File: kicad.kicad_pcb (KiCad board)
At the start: 2 copper layers, 39 parts, among them J1 Screw_Terminal_01x02, J2 Screw_Terminal_01x03, J4 Screw_Terminal_01x03, K1 SANYOU_SRD_Form_C, K2 SANYOU_SRD_Form_C, Q1 BC817, Q2 BC817, Q3 BC817, Q4 BC817, Q5 IRF540N, U1 4N25, U2 4N25, U3 4N25, U4 4N25, U5 LM2575-5.0BT, U6 ACS759xCB-050B-PFF

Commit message: various updates
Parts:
- added C1: 100nF, Capacitor_SMD:C_1206_3216Metric_Pad1.33x1.80mm_HandSolder, F.Cu at (134.6, 96.5)
- added C10: 470uF, Capacitor_SMD:CP_Elec_10x10, F.Cu at (75.9, 70.6)
- added C10A1: ALT, Capacitor_THT:CP_Radial_D10.0mm_P3.80mm, F.Cu at (138.0, 74.8)
- added C11: 470uF, Capacitor_SMD:CP_Elec_10x10, F.Cu at (75.9, 82.5)
- added C11A1: ALT, Capacitor_THT:CP_Radial_D10.0mm_P3.80mm, F.Cu at (141.3, 62.9)
- added C12: 470uF, Capacitor_SMD:CP_Elec_10x10, F.Cu at (92.7, 65.8)
- added C12A1: ALT, Capacitor_THT:CP_Radial_D10.0mm_P3.80mm, F.Cu at (126.2, 74.8)
- added C13: 100uF, Capacitor_THT:CP_Radial_D6.3mm_P2.50mm, F.Cu at (171.9, 105.4)
- added C14: 100nF, Capacitor_SMD:C_1206_3216Metric_Pad1.33x1.80mm_HandSolder, F.Cu at (185.9, 47.3)
- added C15: 100nF, Capacitor_SMD:C_1206_3216Metric_Pad1.33x1.80mm_HandSolder, F.Cu at (177.5, 53.7)
- added C16: 100nF, Capacitor_SMD:C_1206_3216Metric_Pad1.33x1.80mm_HandSolder, F.Cu at (177.5, 57.1)
- added C17: 1nF, Capacitor_SMD:C_1206_3216Metric_Pad1.33x1.80mm_HandSolder, F.Cu at (183.5, 53.7)
- added C18: 100nF, Capacitor_SMD:C_1206_3216Metric_Pad1.33x1.80mm_HandSolder, F.Cu at (217.1, 114.8)
- added C19: 100nF, Capacitor_SMD:C_1206_3216Metric_Pad1.33x1.80mm_HandSolder, F.Cu at (217.1, 118.2)
- added C2: 22pF, Capacitor_SMD:C_1206_3216Metric_Pad1.33x1.80mm_HandSolder, F.Cu at (147.1, 111.6)
- added C20: 100nF, Capacitor_SMD:C_1206_3216Metric_Pad1.33x1.80mm_HandSolder, F.Cu at (195.3, 137.2)
- added C21: 100nF, Capacitor_SMD:C_1206_3216Metric_Pad1.33x1.80mm_HandSolder, F.Cu at (195.3, 133.9)
- added C5A1: ALT, Capacitor_THT:CP_Radial_D10.0mm_P3.80mm, F.Cu at (129.5, 63.2)
- added C6A1: ALT, Capacitor_THT:CP_Radial_D10.0mm_P3.80mm, F.Cu at (114.4, 77.5)
- added C7: 100nF, Capacitor_SMD:C_1206_3216Metric_Pad1.33x1.80mm_HandSolder, F.Cu at (71.6, 90.1)
- added C8: 470uF, Capacitor_SMD:CP_Elec_10x10, F.Cu at (90.0, 77.6)
- added C8A1: ALT, Capacitor_THT:CP_Radial_D10.0mm_P3.80mm, F.Cu at (102.9, 77.5)
- added C9: 470uF, Capacitor_SMD:CP_Elec_10x10, F.Cu at (108.3, 51.5)
- added C9A1: ALT, Capacitor_THT:CP_Radial_D10.0mm_P3.80mm, F.Cu at (133.3, 51.4)
- added D10: LED, LED_SMD:LED_1206_3216Metric, F.Cu at (168.1, 124.6)
- added D11: 1N4007, Diode_THT:D_DO-41_SOD81_P7.62mm_Horizontal, F.Cu at (167.2, 120.7)
- added D12: LED, LED_SMD:LED_1206_3216Metric, F.Cu at (208.1, 81.8)
- added D13: 1N4007, Diode_THT:D_DO-41_SOD81_P7.62mm_Horizontal, F.Cu at (207.1, 77.9)
- added D14: BAT54S, Package_TO_SOT_SMD:SOT-23, F.Cu at (106.8, 140.9)
- added D15: BAT54S, Package_TO_SOT_SMD:SOT-23, F.Cu at (91.6, 140.9)
- added D16: BAT54S, Package_TO_SOT_SMD:SOT-23, F.Cu at (76.4, 140.9)
- added D5: LED, LED_SMD:LED_1206_3216Metric, F.Cu at (229.2, 51.5)
- added D6: LED, LED_SMD:LED_1206_3216Metric, F.Cu at (143.8, 47.3)
- added D7: SS14, Diode_SMD:D_SMA_Handsoldering, F.Cu at (115.3, 85.5)
- added D7A1: ALT, Diode_THT:D_DO-201_P12.70mm_Horizontal, F.Cu at (70.6, 61.3)
- added D8: 1N4007, Diode_THT:D_DO-41_SOD81_P7.62mm_Horizontal, F.Cu at (228.2, 47.7)
- added D9: BAT54S, Package_TO_SOT_SMD:SOT-23, F.Cu at (122.0, 140.9)
- added H1: MountingHole_Pad, MountingHole:MountingHole_4mm_Pad_Via, F.Cu at (161.3, -31.8)
- added H2: MountingHole_Pad, MountingHole:MountingHole_4mm_Pad_Via, F.Cu at (146.1, -31.8)
- added J10: Conn_01x06, Connector_Molex:Molex_KK-254_AE-6410-06A_1x06_P2.54mm_Vertical, F.Cu at (184.9, 122.6)
- added J3: Screw_Terminal_01x03, TerminalBlock:TerminalBlock_bornier-3_P5.08mm, F.Cu at (101.4, 115.2)
- added J5: Screw_Terminal_01x03, TerminalBlock:TerminalBlock_bornier-3_P5.08mm, F.Cu at (101.4, 106.1)
- added J6: USB_B, Connector_USB:USB_B_TE_5787834_Vertical, F.Cu at (153.7, 99.9)
- added J7: Conn_01x03, Connector_Molex:Molex_KK-254_AE-6410-03A_1x03_P2.54mm_Vertical, F.Cu at (206.7, 117.1)
- added J8: Conn_01x03, Connector_Molex:Molex_KK-254_AE-6410-03A_1x03_P2.54mm_Vertical, F.Cu at (184.9, 136.1)
- added J9: Conn_01x03, Connector_Molex:Molex_KK-254_AE-6410-03A_1x03_P2.54mm_Vertical, F.Cu at (167.7, 79.8)
- added JP1: SolderJumper_2_Open, Jumper:SolderJumper-2_P1.3mm_Open_RoundedPad1.0x1.5mm, F.Cu at (107.9, 87.0)
- added JP2: SolderJumper_3_Bridged12, Jumper:SolderJumper-3_P1.3mm_Open_RoundedPad1.0x1.5mm_NumberLabels, F.Cu at (191.8, 47.4)
- added JP3: SolderJumper_2_Bridged, Jumper:SolderJumper-2_P1.3mm_Open_RoundedPad1.0x1.5mm, F.Cu at (235.6, 90.1)
- added JP4: SolderJumper_2_Bridged, Jumper:SolderJumper-2_P1.3mm_Open_RoundedPad1.0x1.5mm, F.Cu at (220.3, 107.1)
- added JP5: SolderJumper_2_Bridged, Jumper:SolderJumper-2_P1.3mm_Open_RoundedPad1.0x1.5mm, F.Cu at (235.6, 76.9)
- added K3: RELAY, Relay_THT:Relay_SPDT_SANYOU_SRD_Series_Form_C, F.Cu at (186.1, 84.3)
- added L1: 68uH, Inductor_SMD:L_12x12mm_H8mm, F.Cu at (57.1, 38.1)
- added L1A1: ALT, Inductor_THT:L_Radial_D12.0mm_P5.00mm_Fastron_11P, F.Cu at (54.6, 38.1)
- added Q6: BC817, Package_TO_SOT_SMD:SOT-23, F.Cu at (167.3, 85.9)
- added Q7: IRF540N, Package_TO_SOT_THT:TO-220-3_Vertical, F.Cu at (157.1, 79.7)
- added Q8: BC817, Package_TO_SOT_SMD:SOT-23, F.Cu at (197.1, 107.6)
- added R15: 1k, Resistor_SMD:R_1206_3216Metric, F.Cu at (183.3, 57.0)
- added R16: 1k, Resistor_SMD:R_1206_3216Metric, F.Cu at (143.8, 50.6)
- added R17: 330, Resistor_SMD:R_1206_3216Metric, F.Cu at (143.8, 53.9)
- added R18: 1k, Resistor_SMD:R_1206_3216Metric, F.Cu at (117.0, 143.6)
- added R19: 1k, Resistor_SMD:R_1206_3216Metric, F.Cu at (117.0, 140.3)
- added R20: 2k, Resistor_SMD:R_1206_3216Metric, F.Cu at (177.3, 60.4)
- added R21: 1k, Resistor_SMD:R_1206_3216Metric, F.Cu at (101.8, 140.3)
- added R22: 1k, Resistor_SMD:R_1206_3216Metric, F.Cu at (101.8, 143.6)
- added R23: 1k, Resistor_SMD:R_1206_3216Metric, F.Cu at (86.6, 140.3)
- added R24: 1k, Resistor_SMD:R_1206_3216Metric, F.Cu at (86.6, 143.6)
- added R25: 1k, Resistor_SMD:R_1206_3216Metric, F.Cu at (71.4, 143.6)
- added R26: 1k, Resistor_SMD:R_1206_3216Metric, F.Cu at (71.4, 140.3)
- added R27: 1k, Resistor_SMD:R_1206_3216Metric, F.Cu at (156.6, 83.4)
- added R28: 10k, Resistor_SMD:R_1206_3216Metric, F.Cu at (162.2, 85.3)
- added R29: 1k, Resistor_SMD:R_1206_3216Metric, F.Cu at (197.7, 103.7)
- added R30: 10k, Resistor_SMD:R_1206_3216Metric, F.Cu at (197.7, 100.4)
- added R31: 1k, Resistor_SMD:R_1206_3216Metric, F.Cu at (236.2, 86.7)
- added R32: 10k, Resistor_SMD:R_1206_3216Metric, F.Cu at (236.2, 83.4)
- added R33: 1k, Resistor_SMD:R_1206_3216Metric, F.Cu at (220.9, 103.7)
- added R34: 10k, Resistor_SMD:R_1206_3216Metric, F.Cu at (220.9, 100.4)
- added R35: 1k, Resistor_SMD:R_1206_3216Metric, F.Cu at (236.2, 73.5)
- added R36: 10k, Resistor_SMD:R_1206_3216Metric, F.Cu at (236.2, 70.2)
- added SW1: SW_Push, Button_Switch_THT:SW_PUSH_6mm, F.Cu at (116.8, 115.0)
- added SW2: SW_Push, Button_Switch_THT:SW_PUSH_6mm, F.Cu at (128.3, 105.9)
- added U10: 4N25, Package_DIP:DIP-6_W7.62mm, F.Cu at (224.2, 70.6)
- added U7: LM2596S-3.3, Package_TO_SOT_SMD:TO-263-5_TabPin3, F.Cu at (77.5, 22.9)
- added U7A1: ALT, Package_TO_SOT_THT:TO-220-5_Vertical, F.Cu at (85.0, 87.5)
- added U8: 4N25, Package_DIP:DIP-6_W7.62mm, F.Cu at (208.9, 100.8)
- added U9: LM7805, Package_TO_SOT_THT:TO-220-3_Vertical, F.Cu at (97.4, 89.2)
- added Y1: 12MHz, Crystal:Crystal_HC49-4H_Vertical, F.Cu at (164.8, 98.2)
- C3: value 100nF -> 22pF
- C5, C6: value 100nF -> 470uF; footprint Capacitor_SMD:C_1206_3216Metric_Pad1.33x1.80mm_HandSolder -> Capacitor_SMD:CP_Elec_10x10
- D1, D2: value 1N4007 -> SS14; footprint Diode_THT:D_DO-41_SOD81_P7.62mm_Horizontal -> Diode_SMD:D_SMA_Handsoldering
- D3: value 1N5822 -> ALT
- D4: value 1N4007 -> ALT; footprint Diode_THT:D_DO-41_SOD81_P7.62mm_Horizontal -> Diode_THT:D_DO-201_P12.70mm_Horizontal
- J4: value Screw_Terminal_01x03 -> Conn_01x05; footprint TerminalBlock:TerminalBlock_bornier-3_P5.08mm -> Connector_Molex:Molex_KK-254_AE-6410-05A_1x05_P2.54mm_Vertical
- K1, K2: value SANYOU_SRD_Form_C -> RELAY
- Q5: value IRF540N -> BC817; footprint Package_TO_SOT_THT:TO-220-3_Vertical -> Package_TO_SOT_SMD:SOT-23
- R1, R13, R2: value 1k -> 10k; footprint Resistor_SMD:R_1206_3216Metric_Pad1.30x1.75mm_HandSolder -> Resistor_SMD:R_1206_3216Metric
- R10, R11, R9: footprint Resistor_SMD:R_1206_3216Metric_Pad1.30x1.75mm_HandSolder -> Resistor_SMD:R_1206_3216Metric
- R12, R14: value 10K -> 10k; footprint Resistor_SMD:R_1206_3216Metric_Pad1.30x1.75mm_HandSolder -> Resistor_SMD:R_1206_3216Metric
- R3: value 22k -> 1k; footprint Resistor_SMD:R_0805_2012Metric_Pad1.20x1.40mm_HandSolder -> Resistor_SMD:R_1206_3216Metric
- R4: value 5k6 -> 1k; footprint Resistor_SMD:R_0805_2012Metric_Pad1.20x1.40mm_HandSolder -> Resistor_SMD:R_1206_3216Metric
- R5: value 10k -> 22k; footprint Resistor_SMD:R_1206_3216Metric_Pad1.30x1.75mm_HandSolder -> Resistor_SMD:R_1206_3216Metric
- R6: value 10k -> 5k6; footprint Resistor_SMD:R_1206_3216Metric_Pad1.30x1.75mm_HandSolder -> Resistor_SMD:R_1206_3216Metric
- R7, R8: value 10k -> 1k; footprint Resistor_SMD:R_1206_3216Metric_Pad1.30x1.75mm_HandSolder -> Resistor_SMD:R_1206_3216Metric
- U1: value 4N25 -> CH340G; footprint Package_DIP:DIP-6_W7.62mm -> Package_SO:SOIC-16_3.9x9.9mm_P1.27mm
- U2: value 4N25 -> ACS759; footprint Package_DIP:DIP-6_W7.62mm -> Sensor_Current:Allegro_CB_PFF
- U3: value 4N25 -> ACS712; footprint Package_DIP:DIP-6_W7.62mm -> Package_SO:SOIC-8_3.9x4.9mm_P1.27mm
- U5: value LM2575-5.0BT -> 4N25; footprint Package_TO_SOT_THT:TO-220-5_Vertical -> Package_DIP:DIP-6_W7.62mm
- U6: value ACS759xCB-050B-PFF -> ESP32; footprint Sensor_Current:Allegro_CB_PFF -> RF_Module:ESP32-WROOM-32
- moved RV1 155.5 mm to (77.5, 90.0)
- moved U3 149.2 mm to (153.7, -14.0), turned to 270 degrees
- moved U2 146.5 mm to (151.7, 0.00)
- moved D3 135.9 mm to (70.6, 130.8)
- moved R5 132.1 mm to (103.0, 130.5)
- moved C6 131.3 mm to (106.8, 65.8)
- moved C5 122.2 mm to (122.4, 51.5)
- moved R2 115.9 mm to (114.2, 132.7)
- moved J1 104.4 mm to (118.0, 108.4)
- moved R11 104.2 mm to (108.6, 132.7)
- moved R6 104.0 mm to (103.0, 133.8)
- moved D1 97.0 mm to (103.1, 122.0)
- moved J4 96.9 mm to (87.7, 131.3)
- moved R3 93.5 mm to (234.8, 51.5)
- moved D4 93.2 mm to (100.2, 98.2)
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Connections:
- net Net-(J2-Pad1) renamed /Relay 1/NO
- net Net-(J2-Pad2) renamed /Relay 1/COM
- net Net-(J2-Pad3) renamed /Relay 1/NC
- C3 pad 1: +3V3 -> Net-(C3-Pad1)
- C4 pad 1: /TBAT -> +3V3
- C5 pad 1: Net-(C5-Pad1) -> +12V
- C6 pad 1: /TEMP2 -> +12V
- D1 pad 2: Net-(D1-Pad2) -> VUSB
- D3 pad 1: Net-(D3-Pad1) -> +12V
- D3 pad 2: GND -> Net-(D2-Pad2)
- D4 pad 2: Net-(D4-Pad2) -> VUSB
- J1 pad 1: Net-(D1-Pad2) -> Net-(D2-Pad2)
- J4 pad 1: Net-(J4-Pad1) -> SCL
- J4 pad 2: Net-(J4-Pad2) -> SDA
- J4 pad 3: Net-(J4-Pad3) -> +3V3
- K1 pad 2: Net-(D2-Pad2) -> Net-(D8-Pad2)
- K2 pad 1: Net-(J4-Pad2) -> /Relay 2/COM
- K2 pad 2: Net-(D4-Pad2) -> Net-(D11-Pad2)
- K2 pad 3: Net-(J4-Pad1) -> /Relay 2/NO
- K2 pad 4: Net-(J4-Pad3) -> /Relay 2/NC
- Q1 pad 3: Net-(Q1-Pad3) -> Net-(D8-Pad2)
- Q2 pad 3: Net-(D2-Pad2) -> Net-(D11-Pad2)
- Q3 pad 3: Net-(D4-Pad2) -> Net-(D13-Pad2)
- Q4 pad 2: GND -> Net-(Q4-Pad2)
- Q4 pad 3: Net-(Q4-Pad3) -> GPIO0
- Q5 pad 1: Net-(Q4-Pad3) -> Net-(Q5-Pad1)
- Q5 pad 2: Net-(J5-Pad3) -> Net-(Q5-Pad2)
- Q5 pad 3: GND -> RESET
- R1 pad 1: Net-(Q1-Pad1) -> +3V3
- R1 pad 2: /UPS_ON -> RESET
- R10 pad 1: Net-(Q4-Pad1) -> Net-(Q3-Pad1)
- R10 pad 2: /FAN_1 -> RELAY_3
- R11 pad 1: +12V -> +3V3
- R11 pad 2: Net-(Q4-Pad3) -> SDA
- R12 pad 2: /SDA -> SCL
- R13 pad 1: /IBAT -> Net-(Q4-Pad1)
- R13 pad 2: Net-(C5-Pad1) -> Net-(Q5-Pad2)
- R14 pad 1: +3V3 -> Net-(Q5-Pad1)
- R14 pad 2: /SCL -> Net-(Q4-Pad2)
- R2 pad 1: Net-(Q2-Pad1) -> +3V3
- R2 pad 2: /RELAY_1 -> GPIO0
- R3 pad 1: +12V -> Net-(D5-Pad1)
- R3 pad 2: /VBAT -> Net-(D8-Pad2)
- R4 pad 1: /VBAT -> Net-(Q1-Pad1)
- R4 pad 2: GND -> RELAY_1
- R5 pad 1: +3V3 -> +12V
- R5 pad 2: Net-(Q1-Pad3) -> /Input Protection/IN
- R6 pad 1: /UPS_NORMAL -> /Input Protection/IN
- R6 pad 2: +3V3 -> GND
- R7 pad 1: /UPS_CARGA -> Net-(D10-Pad1)
- R7 pad 2: +3V3 -> Net-(D11-Pad2)
- R8 pad 1: /UPS_INVERTER -> Net-(Q2-Pad1)
- R8 pad 2: +3V3 -> RELAY_2
- R9 pad 1: Net-(Q3-Pad1) -> Net-(D12-Pad1)
- R9 pad 2: /RELAY_2 -> Net-(D13-Pad2)
- U1 pad 1: Net-(Q1-Pad3) -> GND
- U1 pad 2: GND -> RXD0
- U1 pad 3: Net-(U1-Pad3) -> TXD0
- U1 pad 4: Net-(J3-Pad2) -> +3V3
- U2 pad 1: Net-(J3-Pad4) -> +3V3
- U2 pad 2: Net-(J3-Pad3) -> GND
- U2 pad 4: GND -> /Current Sensor/IP+
- U2 pad 5: /UPS_NORMAL -> /Current Sensor/IP-
- U3 pad 1: Net-(J3-Pad4) -> /Current Sensor/IP+
- U3 pad 2: Net-(J3-Pad5) -> /Current Sensor/IP+
- U3 pad 3: Net-(U3-Pad3) -> /Current Sensor/IP-
- U3 pad 4: GND -> /Current Sensor/IP-
- U3 pad 5: /UPS_CARGA -> GND
- U4 pad 1: Net-(J3-Pad4) -> Net-(Q8-Pad3)
- U4 pad 2: Net-(J3-Pad6) -> GND
- U4 pad 4: GND -> /Interfaz UPS/Salida UPS_ON/E
- U4 pad 5: /UPS_INVERTER -> /Interfaz UPS/Salida UPS_ON/C
- U5 pad 1: +12V -> Net-(JP3-Pad2)
- U5 pad 2: Net-(D3-Pad1) -> /Interfaz UPS/Entrada UPS_NORMAL/K
- U5 pad 3: GND -> Net-(U5-Pad3)
- U5 pad 4: Net-(JP1-Pad2) -> GND
- U5 pad 5: GND -> UPS_NORMAL
- U6 pad 1: +3V3 -> GND
- U6 pad 2: GND -> +3V3
- U6 pad 3: Net-(C5-Pad1) -> RESET
- U6 pad 4: Net-(H1-Pad1) -> VBAT
- U6 pad 5: Net-(H2-Pad1) -> TBAT

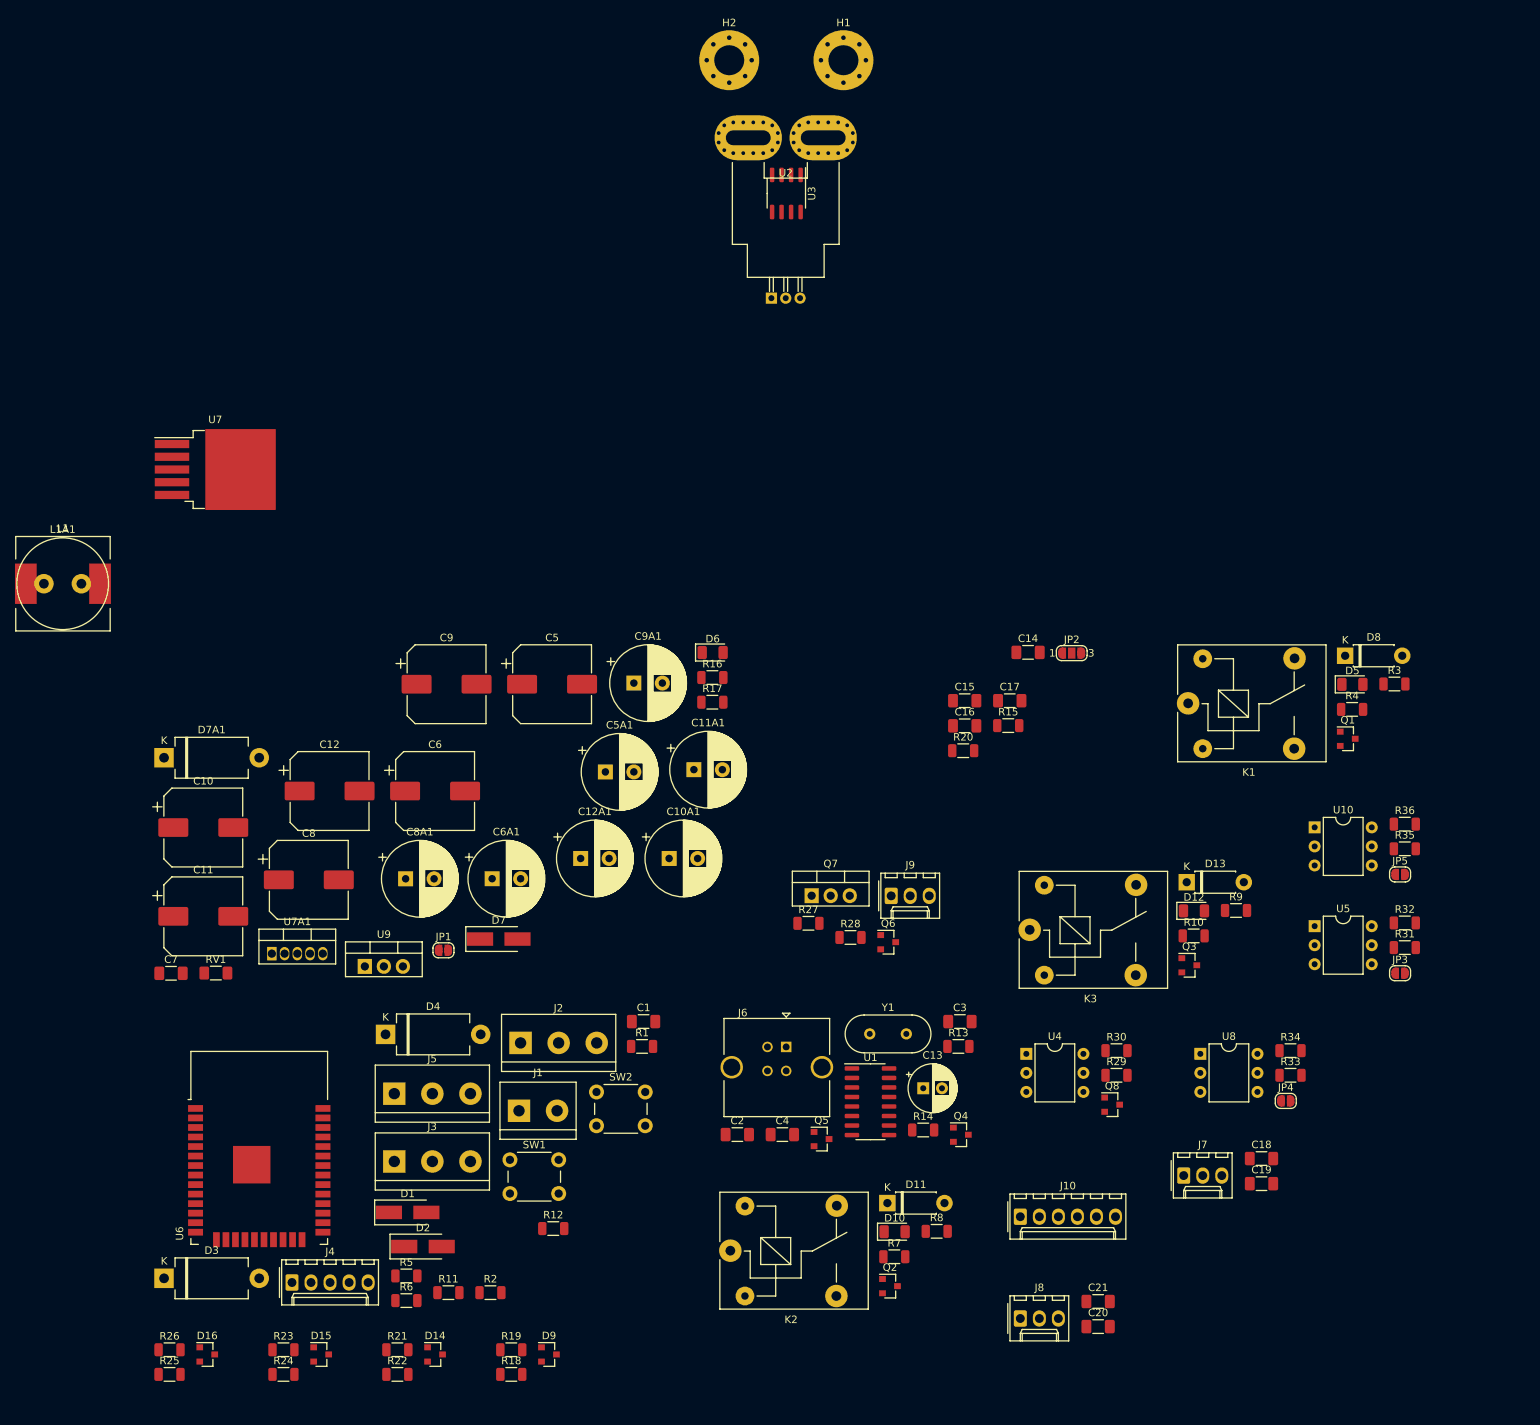
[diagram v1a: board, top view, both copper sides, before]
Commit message: more footprints & 3d models
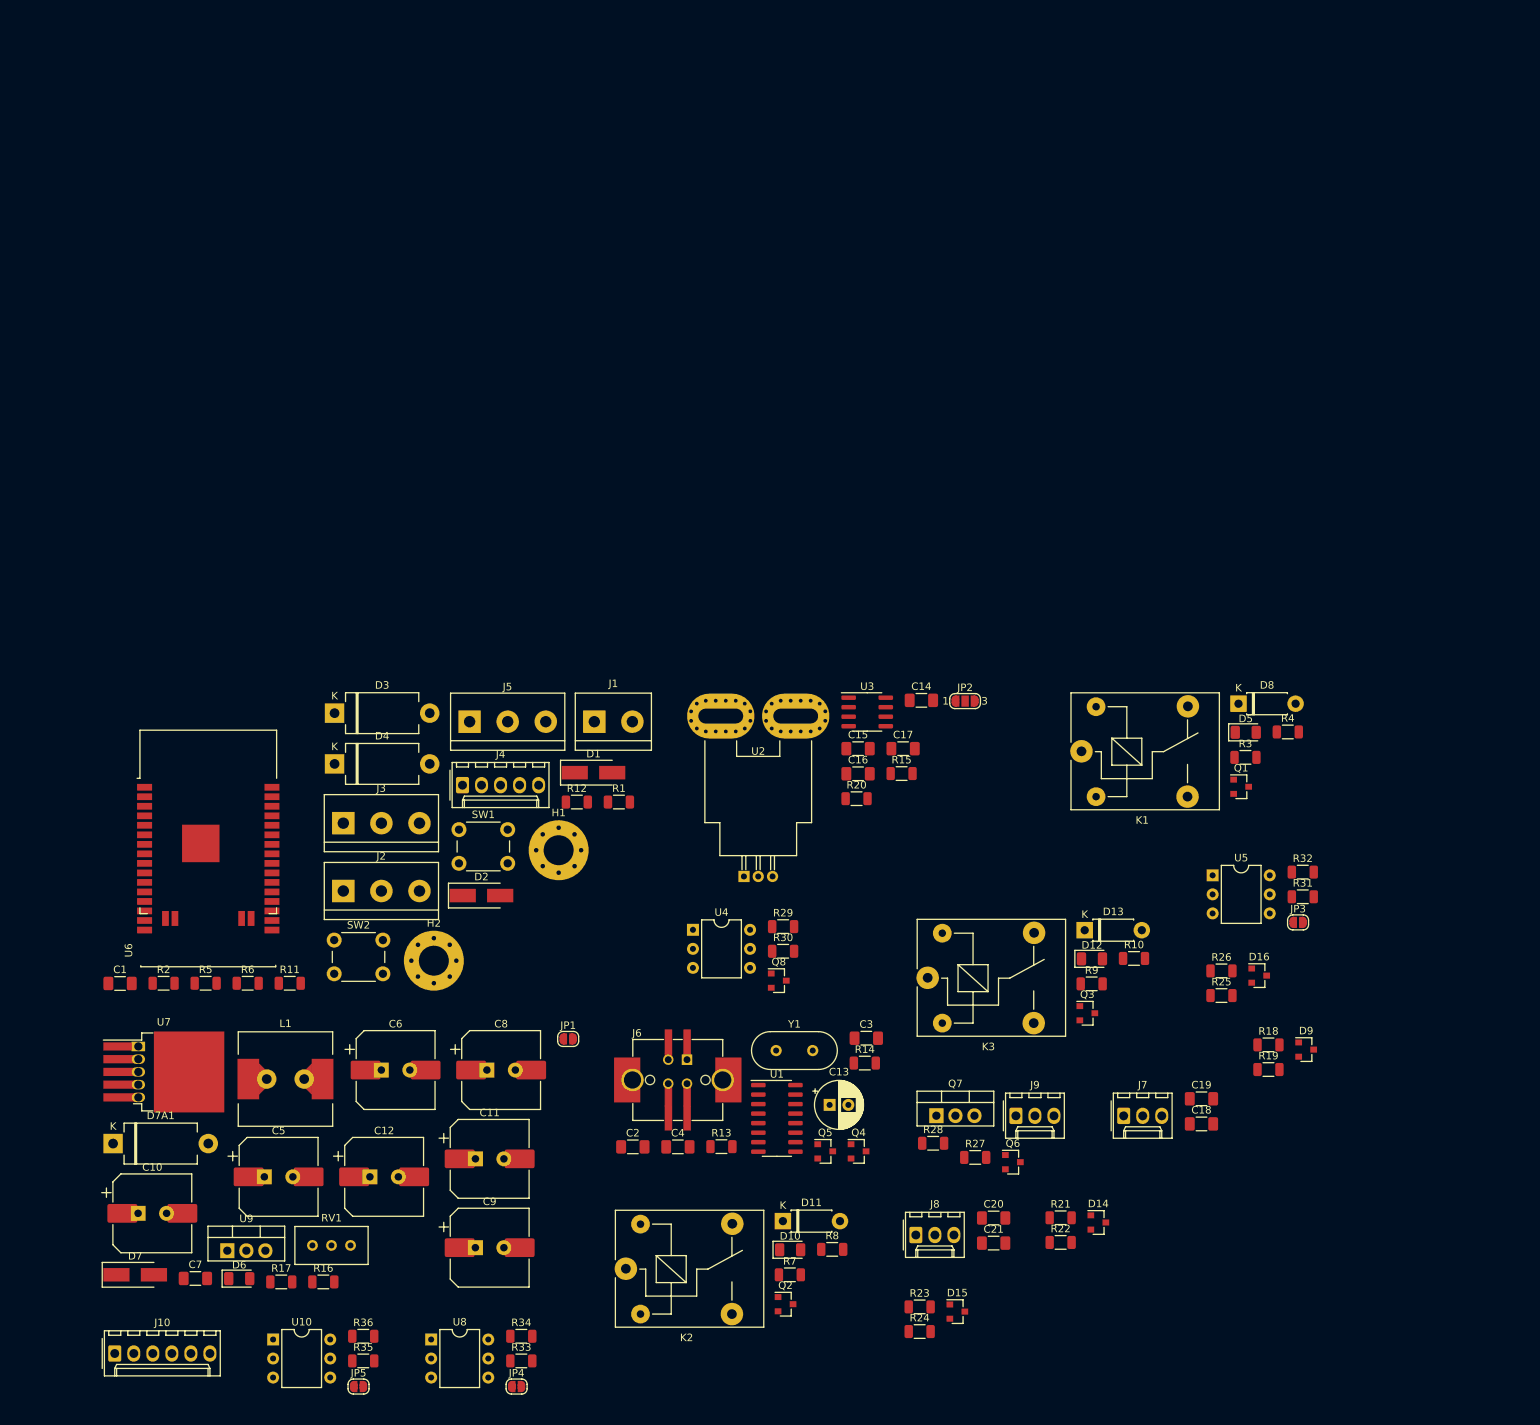
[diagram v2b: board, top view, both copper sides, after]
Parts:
- removed C10A1, C11A1, C12A1, C5A1, C6A1, C8A1, C9A1: ALT, Capacitor_THT:CP_Radial_D10.0mm_P3.80mm
- removed L1A1: ALT, Inductor_THT:L_Radial_D12.0mm_P5.00mm_Fastron_11P
- removed U7A1: ALT, Package_TO_SOT_THT:TO-220-5_Vertical
- C10, C11, C12, C5, C6, C8, C9: footprint Capacitor_SMD:CP_Elec_10x10 -> libs:CAP_10x10_SMD_THT
- J1: footprint TerminalBlock:TerminalBlock_bornier-2_P5.08mm -> libs:TerminalBlock_bornier-2_P5.08mm
- J2, J3, J5: footprint TerminalBlock:TerminalBlock_bornier-3_P5.08mm -> libs:TerminalBlock_bornier-3_P5.08mm
- J6: footprint Connector_USB:USB_B_TE_5787834_Vertical -> libs:USB-B-VERTICAL-SMD&THT
- L1: footprint Inductor_SMD:L_12x12mm_H8mm -> libs:L_12x12mm_H8mm
- RV1: footprint Resistor_SMD:R_1206_3216Metric_Pad1.30x1.75mm_HandSolder -> Potentiometer_THT:Potentiometer_Bourns_3296W_Vertical
- U2: footprint Sensor_Current:Allegro_CB_PFF -> libs:Allegro_CB_PFF
- U6: footprint RF_Module:ESP32-WROOM-32 -> esp32-wroom-roover:ESP32-WROOM-WROVER-NC
- U7: footprint Package_TO_SOT_SMD:TO-263-5_TabPin3 -> libs:TO-263-5_TabPin3
- moved R35 154.9 mm to (97.2, 141.8)
- moved JP5 154.9 mm to (96.6, 145.2)
- moved R36 154.9 mm to (97.2, 138.5)
- moved U10 154.9 mm to (85.2, 138.9)
- moved D16 149.2 mm to (216.8, 90.4)
- moved R25 149.2 mm to (211.7, 93.0)
- moved R26 149.2 mm to (211.7, 89.8)
- moved H2 126.4 mm to (106.6, 88.4)
- moved J10 122.2 mm to (64.1, 140.8)
- moved H1 112.1 mm to (123.3, 73.7)
- moved R18 110.2 mm to (218.0, 99.6)
- moved JP4 109.5 mm to (117.7, 145.2)
- moved R33 109.5 mm to (118.3, 141.8)
- moved R34 109.5 mm to (118.3, 138.5)
- moved U8 109.5 mm to (106.3, 138.9)
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
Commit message: Several changes
Usando stock de http://tienda.ityt.com.ar/
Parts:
- removed D3, D4, D7A1: ALT, Diode_THT:D_DO-201_P12.70mm_Horizontal
- removed Q8: BC817, Package_TO_SOT_SMD:SOT-23
- removed R36: 10k, Resistor_SMD:R_1206_3216Metric
- added J11: ICSP, Connector_PinSocket_2.54mm:PinSocket_1x06_P2.54mm_Vertical, F.Cu at (179.3, 98.3)
- added U11: DS1233A-10, Package_TO_SOT_THT:TO-92, F.Cu at (123.8, 89.0)
- D11, D13, D8: value 1N4007 -> M7; footprint Diode_THT:D_DO-41_SOD81_P7.62mm_Horizontal -> Diode_SMD:D_SMA_Handsoldering
- Q7: value IRF540N -> IRLML2502; footprint Package_TO_SOT_THT:TO-220-3_Vertical -> Package_TO_SOT_SMD:SOT-23
- R29: value 1k -> 100
- R30, R32, R34: value 10k -> 1k
- R31, R33, R35: value 1k -> 10k
- U10, U4, U5, U8: value 4N25 -> PC817XI; footprint Package_DIP:DIP-6_W7.62mm -> Package_DIP:SMDIP-4_W9.53mm
- U9: value LM7805 -> AMS1117-5.0; footprint Package_TO_SOT_THT:TO-220-3_Vertical -> Package_TO_SOT_SMD:SOT-223-3_TabPin2
- moved R18 129.3 mm to (95.0, 139.8)
- moved D9 128.3 mm to (100.1, 137.1)
- moved R19 127.4 mm to (95.0, 136.5)
- moved Q2 123.8 mm to (250.8, 57.5)
- moved D11 117.9 mm to (247.9, 53.0)
- moved K2 115.4 mm to (223.8, 59.2)
- moved R7 115.3 mm to (245.7, 60.3)
- moved D10 115.3 mm to (245.8, 57.0)
- moved U8 107.2 mm to (208.1, 105.3)
- moved R35 107.0 mm to (186.3, 82.6)
- moved U10 106.8 mm to (176.9, 84.3)
- moved R8 106.7 mm to (245.7, 63.6)
- moved R33 106.2 mm to (217.4, 103.7)
- moved J10 105.0 mm to (124.1, 54.7)
- moved U4 102.4 mm to (243.2, 75.1)
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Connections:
- net /Interfaz UPS/Entrada UPS_CARGA/K renamed /opto-in-2/K
- net /Interfaz UPS/Entrada UPS_INVERTER/K renamed /opto-in-3/K
- net /Interfaz UPS/Entrada UPS_NORMAL/K renamed /opto-in-1/K
- net Net-(D2-Pad2) renamed +BATT
- J10 pad 1: /Interfaz UPS/Salida UPS_ON/C -> /opto-out-1/C
- J10 pad 2: /Interfaz UPS/Salida UPS_ON/E -> /opto-out-1/E
- J10 pad 4: /Interfaz UPS/Entrada UPS_CARGA/A -> /opto-in-1/A
- J9 pad 3: Net-(J9-Pad3) -> /Salida MOSFET/OUT
- JP3 pad 1: /Interfaz UPS/Entrada UPS_CARGA/A -> /opto-in-1/A
- JP4 pad 1: /Interfaz UPS/Entrada UPS_CARGA/A -> /opto-in-1/A
- JP5 pad 1: /Interfaz UPS/Entrada UPS_CARGA/A -> /opto-in-1/A
- Q7 pad 2: Net-(J9-Pad3) -> GND
- Q7 pad 3: GND -> /Salida MOSFET/OUT
- R15 pad 2: GND -> Net-(R15-Pad2)
- R20 pad 1: Net-(R20-Pad1) -> GND
- R29 pad 1: Net-(Q8-Pad1) -> Net-(R29-Pad1)
- R29 pad 2: UPS_ON -> OUT0
- R30 pad 1: +3V3 -> Net-(JP3-Pad2)
- R30 pad 2: Net-(Q8-Pad3) -> /opto-in-1/A
- R31 pad 1: Net-(JP3-Pad2) -> +3V3
- R31 pad 2: /Interfaz UPS/Entrada UPS_CARGA/A -> IN0
- R32 pad 1: +3V3 -> Net-(JP4-Pad2)
- R32 pad 2: UPS_NORMAL -> /opto-in-1/A
- R33 pad 1: Net-(JP4-Pad2) -> +3V3
- R33 pad 2: /Interfaz UPS/Entrada UPS_CARGA/A -> IN1
- R34 pad 1: +3V3 -> Net-(JP5-Pad2)
- R34 pad 2: UPS_CARGA -> /opto-in-1/A
- R35 pad 1: Net-(JP5-Pad2) -> +3V3
- R35 pad 2: /Interfaz UPS/Entrada UPS_CARGA/A -> IN2
- U10 pad 3: Net-(U10-Pad3) -> GND
- U10 pad 4: GND -> IN2
- U3 pad 7: Net-(R20-Pad1) -> Net-(R15-Pad2)
- U4 pad 1: Net-(Q8-Pad3) -> +3V3
- U4 pad 2: GND -> Net-(R29-Pad1)
- U4 pad 3: Net-(U4-Pad3) -> /opto-out-1/E
- U4 pad 4: /Interfaz UPS/Salida UPS_ON/E -> /opto-out-1/C
- U5 pad 3: Net-(U5-Pad3) -> GND
- U5 pad 4: GND -> IN0
- U8 pad 3: Net-(U8-Pad3) -> GND
- U8 pad 4: GND -> IN1
- U9 pad 1: +12V -> GND
- U9 pad 2: GND -> +5V
- U9 pad 3: +5V -> +12V
